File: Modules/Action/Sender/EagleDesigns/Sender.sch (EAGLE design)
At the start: 10 parts, among them U2 ATMEGA328P_TQFP

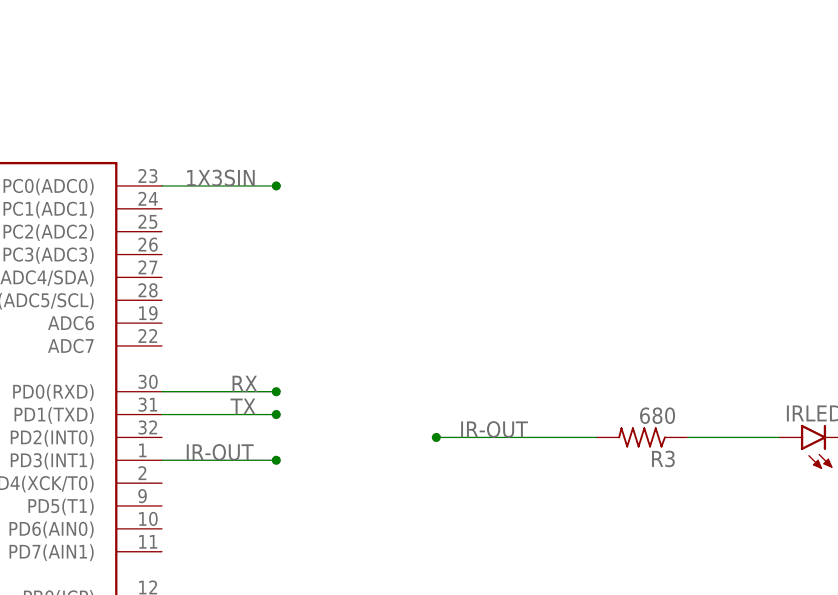
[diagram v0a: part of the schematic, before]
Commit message: fixed eagle files for new modules
SIN/SOUT was not correctly connected in them.
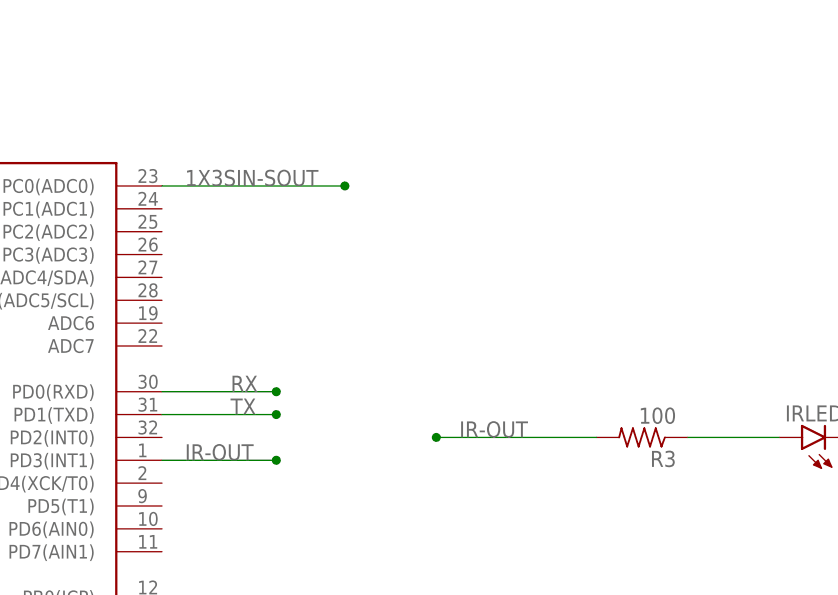
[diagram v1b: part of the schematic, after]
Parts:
- R3: value 680 -> 100
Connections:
- removed net 1X3SIN: U2.PC0(ADC0)
- net 1X3SIN-SOUT: now also U2.PC0(ADC0)
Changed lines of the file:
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@@
 <part name="C2" library="adafruit" deviceset="C-US" device="C0603" value="22pF"/>
 <part name="GND3" library="SparkFun-Aesthetics" deviceset="GND" device=""/>
-<part name="R3" library="adafruit" deviceset="R-US_" device="R0603" value="680"/>
+<part name="R3" library="adafruit" deviceset="R-US_" device="R0603" value="100"/>
 <part name="IRLED" library="SparkFun-LED" deviceset="LED" device="5MM"/>
 </parts>
@@
 <pinref part="R1" gate="G$1" pin="2"/>
 </segment>
+<segment>
+<pinref part="U2" gate="U$1" pin="PC0(ADC0)"/>
+<wire x1="208.28" y1="55.88" x2="228.6" y2="55.88" width="0.1524" layer="91"/>
+<junction x="228.6" y="55.88"/>
+<label x="210.82" y="55.88" size="1.778" layer="95"/>
+</segment>
 </net>
 <net name="RESET" class="0">
@@
 </segment>
 </net>
-<net name="1X3SIN" class="0">
-<segment>
-<pinref part="U2" gate="U$1" pin="PC0(ADC0)"/>
-<wire x1="208.28" y1="55.88" x2="220.98" y2="55.88" width="0.1524" layer="91"/>
-<junction x="220.98" y="55.88"/>
-<label x="210.82" y="55.88" size="1.778" layer="95"/>
-</segment>
-</net>

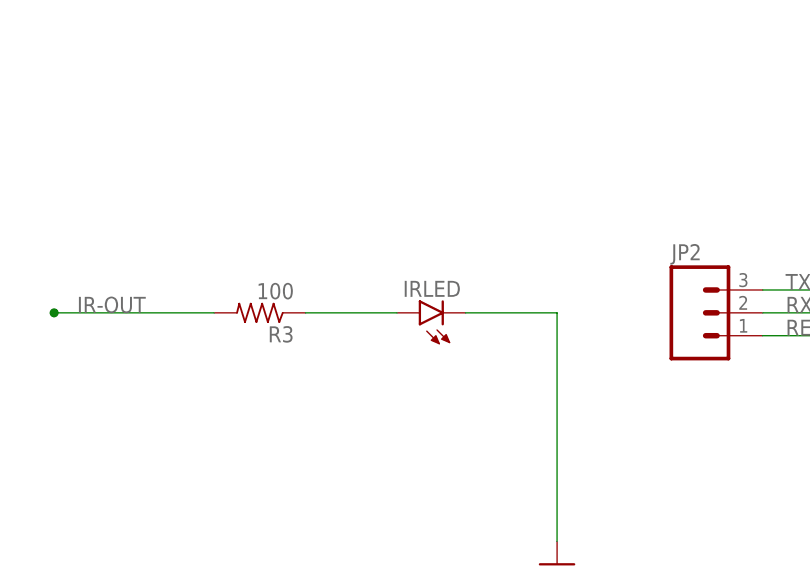
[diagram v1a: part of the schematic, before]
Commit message: Sender: added final PCB #29
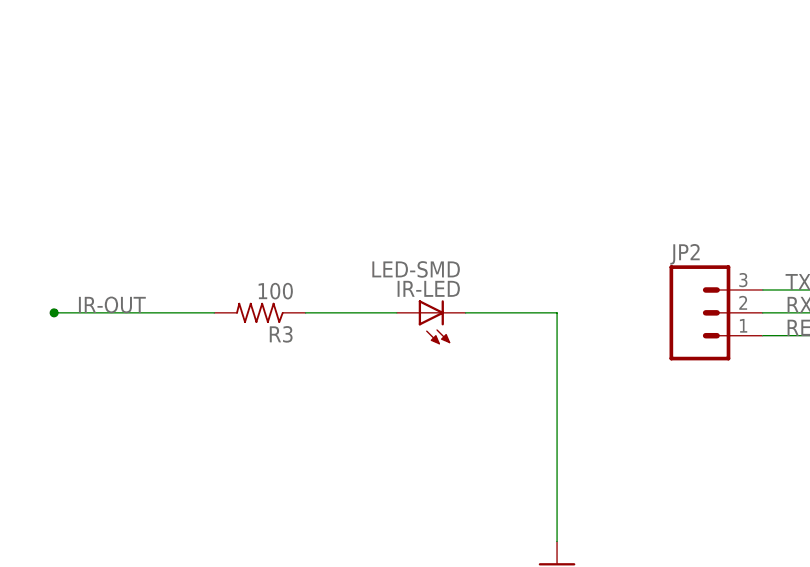
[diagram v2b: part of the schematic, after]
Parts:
- removed IRLED: (no value), SparkFun-LED:LED5MM
- added IR-LED: LED-SMD, MakerWear:LED-SMD
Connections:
- net GND: now also IR-LED.C; no longer IRLED.C
- net N$2: now also IR-LED.A; no longer IRLED.A
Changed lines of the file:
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@@
 <part name="GND3" library="SparkFun-Aesthetics" deviceset="GND" device=""/>
 <part name="R3" library="adafruit" deviceset="R-US_" device="R0603" value="100"/>
-<part name="IRLED" library="SparkFun-LED" deviceset="LED" device="5MM"/>
+<part name="IR-LED" library="MakerWear" deviceset="LED-SMD" device=""/>
 </parts>
 <sheets>
@@
 <instance part="GND3" gate="1" x="294.64" y="0"/>
 <instance part="R3" gate="G$1" x="261.62" y="27.94" rot="R180"/>
-<instance part="IRLED" gate="G$1" x="279.4" y="27.94" rot="R90"/>
+<instance part="IR-LED" gate="G$1" x="281.94" y="27.94" rot="R90"/>
 </instances>
 <busses>
@@
 <wire x1="294.64" y1="2.54" x2="294.64" y2="27.94" width="0.1524" layer="91"/>
 <wire x1="284.48" y1="27.94" x2="294.64" y2="27.94" width="0.1524" layer="91"/>
-<pinref part="IRLED" gate="G$1" pin="C"/>
+<pinref part="IR-LED" gate="G$1" pin="C"/>
 </segment>
 </net>
@@
 <wire x1="276.86" y1="27.94" x2="266.7" y2="27.94" width="0.1524" layer="91"/>
 <pinref part="R3" gate="G$1" pin="1"/>
-<pinref part="IRLED" gate="G$1" pin="A"/>
-</segment>
-</net>
+<pinref part="IR-LED" gate="G$1" pin="A"/>
+</segment>
+</net>

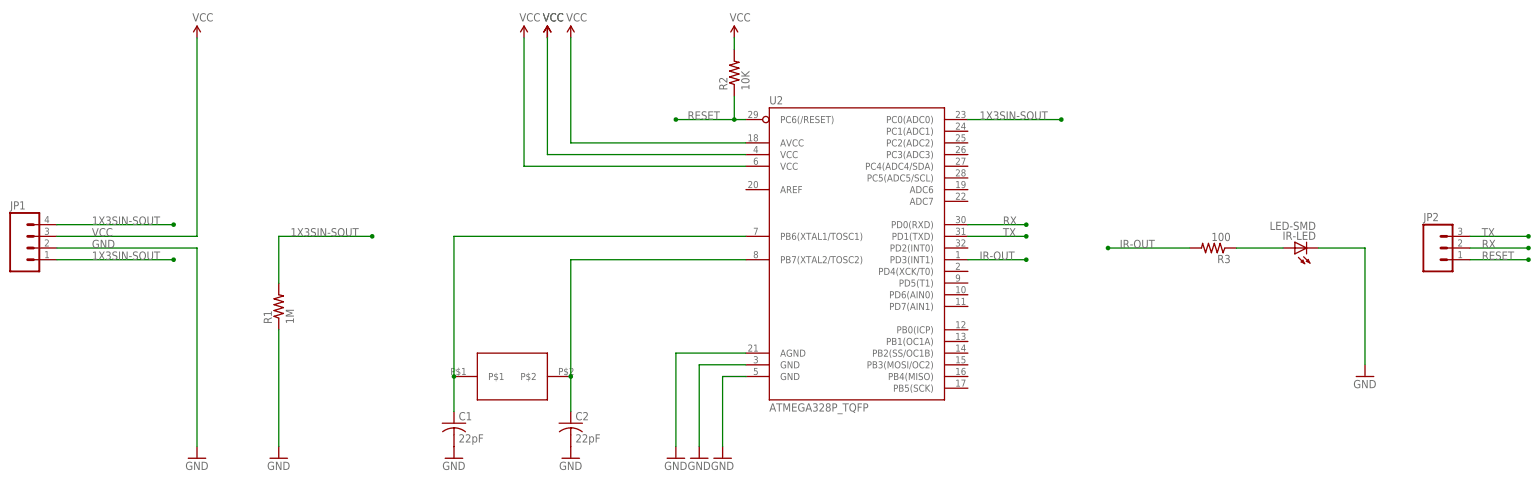
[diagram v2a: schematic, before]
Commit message: Sender: removed crystal, modified to work with new bootloader
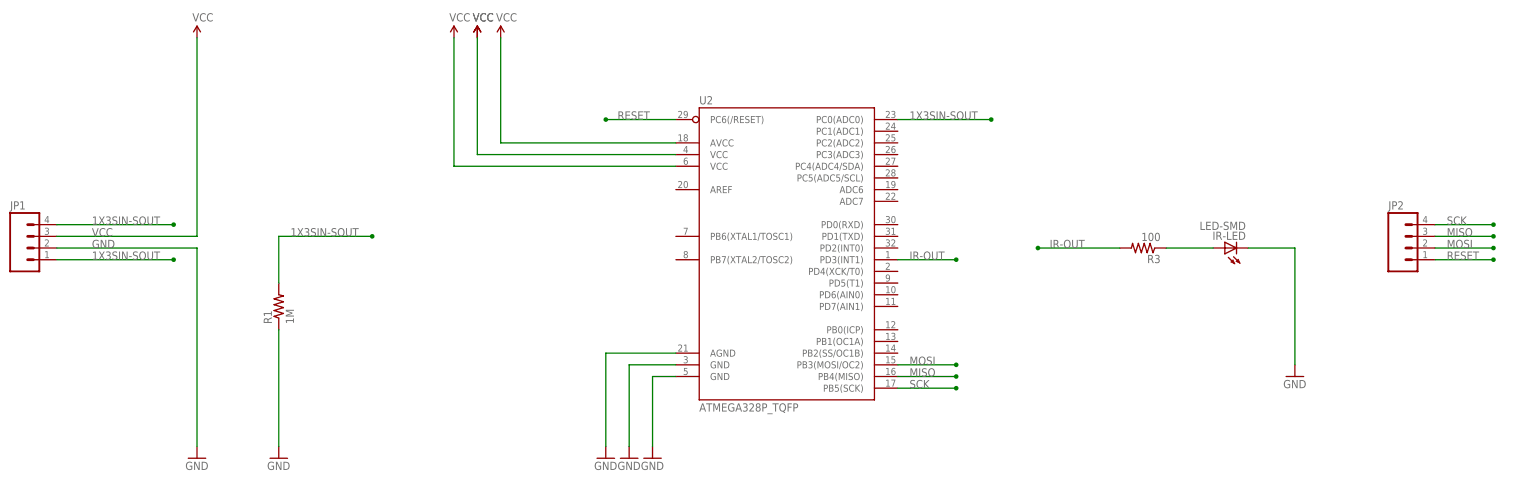
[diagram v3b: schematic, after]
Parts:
- removed C1, C2: 22pF, adafruit:C-USC0603
- removed R2: 10K, resistor:R-US_R0603
- removed U$2: NX503, MakerWear:NX503
- JP2: device SparkFun-Connectors:M03PTH -> SparkFun-Connectors:M04PTH
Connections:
- removed net N$1: C1.1, U$2.P$1, U2.PB6(XTAL1/TOSC1)
- removed net N$3: C2.1, U$2.P$2, U2.PB7(XTAL2/TOSC2)
- removed net RX: JP2.2, U2.PD0(RXD)
- removed net TX: JP2.3, U2.PD1(TXD)
- new net MISO: JP2.3, U2.PB4(MISO)
- new net MOSI: JP2.2, U2.PB3(MOSI/OC2)
- new net SCK: JP2.4, U2.PB5(SCK)
- net GND: no longer C1.2, C2.2
- net RESET: no longer R2.1
- net VCC: no longer R2.2
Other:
- moved on the sheet: IR-LED, R3, U2
